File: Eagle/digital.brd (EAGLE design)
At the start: 111.1 x 67.3 mm, 53 parts, among them IC1 MAX232, J1 USB+SHIELD

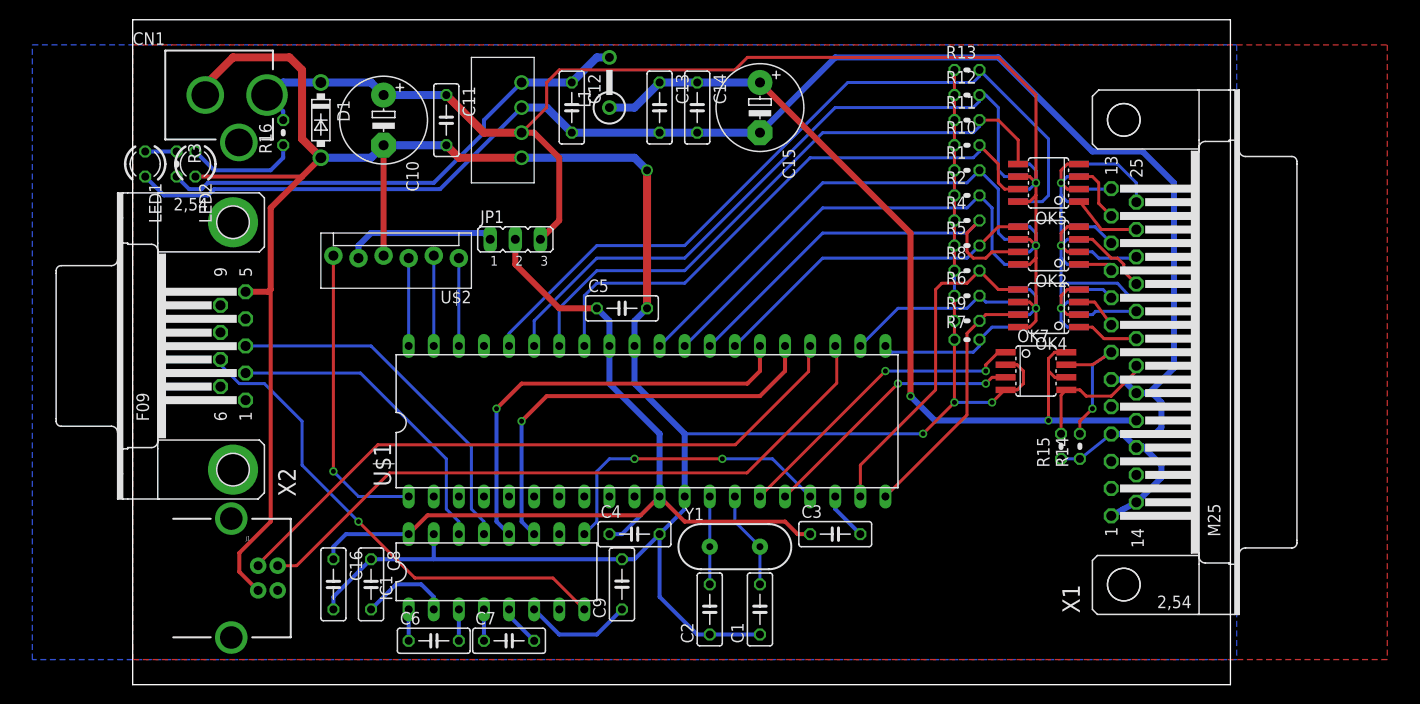
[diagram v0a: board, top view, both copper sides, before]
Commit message: Added connection monitor
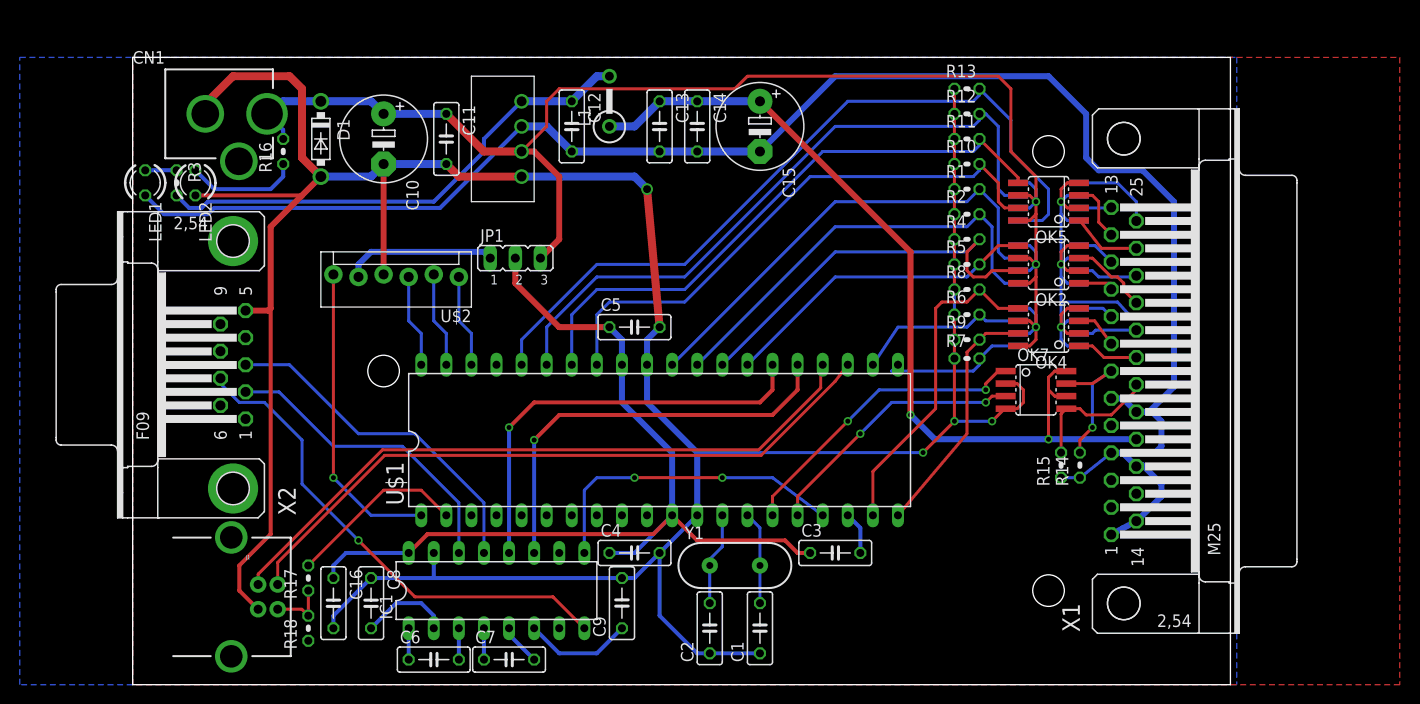
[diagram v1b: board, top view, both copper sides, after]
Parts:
- added R17, R18: 100k, resistor:0204V
- moved U$1 2.29 mm to (53.3, 24.8)
- moved C5 2.29 mm to (50.8, 36.2)
- moved C10 1.91 mm to (25.4, 55.2)
- moved C11 1.91 mm to (31.8, 55.2)
- moved C12 1.91 mm to (44.5, 56.5)
- moved C13 1.91 mm to (53.3, 56.5)
- moved C14 1.91 mm to (57.1, 56.5)
- moved C15 1.91 mm to (63.5, 56.5)
- moved CN1 1.91 mm to (0.00, 57.8)
- moved D1 1.91 mm to (19.1, 55.2)
- moved JP1 1.91 mm to (38.7, 43.2)
- moved L1 1.91 mm to (48.3, 59.1)
- moved LED1 1.91 mm to (1.27, 50.8)
- moved LED2 1.91 mm to (6.35, 50.8)
- moved OK1 1.91 mm to (92.7, 42.5)
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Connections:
- new net N$42: J1.VBUS, R17.1, R18.2
- new net N$55: R17.2, U$1.2
- net DGND: now also R18.1
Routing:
- net N$55: track 0.00 -> 18.2 mm
- net N$42: track 0.00 -> 5.91 mm
- net GND: track 228.0 -> 230.6 mm
- net N$45: track 94.2 -> 96.7 mm
- net N$4: track 30.6 -> 32.3 mm
- net N$34: track 61.8 -> 60.2 mm
- net USB_P: track 66.7 -> 68.2 mm
- net N$53: track 36.5 -> 35.0 mm
- net N$33: track 58.6 -> 57.4 mm
- net N$25: track 42.0 -> 40.7 mm
- net N$27: track 33.7 -> 32.4 mm
- net N$24: track 45.6 -> 44.3 mm
- net N$15: track 49.2 -> 47.9 mm
- net N$31: track 25.9 -> 25.0 mm
- net N$29: track 18.3 -> 17.5 mm
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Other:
- board size 111.1 x 67.3 mm -> 111.1 x 63.5 mm

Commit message: Board updates
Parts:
- moved R3 17.2 mm to (21.6, 49.5), turned to 0 degrees
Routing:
- net N$26: track 50.6 -> 31.7 mm
- net N$28: track 3.18 -> 21.5 mm
- net DGND: track 300.1 -> 293.9 mm, vias 4 -> 3
- net +5V/2: track 156.0 -> 153.7 mm
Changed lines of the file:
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@@
 <element name="C11" library="resistor" package="C050-025X075" value="0.1uF" x="31.75" y="55.245" rot="R270"/>
 <element name="U$3" library="modEEG" package="SIP4" value="ROL-0505S" x="38.1" y="55.245" rot="R90"/>
-<element name="R3" library="resistor" package="0204V" value="1.65k" x="4.445" y="50.8" rot="R270"/>
+<element name="R3" library="resistor" package="0204V" value="1.65k" x="21.59" y="49.53"/>
 <element name="LED1" library="led" package="LED3MM" value="" x="1.27" y="50.8" rot="R270"/>
 <element name="C12" library="resistor" package="C050-025X075" value="0.1uF" x="44.45" y="56.515" rot="R270"/>
@@
 <contactref element="R3" pad="1"/>
 <contactref element="LED1" pad="A"/>
-<wire x1="1.27" y1="52.07" x2="4.445" y2="52.07" width="0.4064" layer="16"/>
+<wire x1="20.32" y1="49.53" x2="8.255" y2="49.53" width="0.4064" layer="16"/>
+<wire x1="8.255" y1="49.53" x2="6.985" y2="48.26" width="0.4064" layer="16"/>
+<wire x1="6.985" y1="48.26" x2="4.445" y2="48.26" width="0.4064" layer="16"/>
+<wire x1="4.445" y1="48.26" x2="2.54" y2="50.165" width="0.4064" layer="16"/>
+<wire x1="2.54" y1="50.165" x2="2.54" y2="50.8" width="0.4064" layer="16"/>
+<wire x1="2.54" y1="50.8" x2="1.27" y2="52.07" width="0.4064" layer="16"/>
 </signal>
 <signal name="DGND">
@@
 <wire x1="31.75" y1="52.705" x2="33.02" y2="51.435" width="0.8128" layer="1"/>
 <wire x1="33.02" y1="51.435" x2="39.37" y2="51.435" width="0.8128" layer="1"/>
-<wire x1="39.37" y1="51.435" x2="50.8" y2="51.435" width="0.8128" layer="16"/>
-<wire x1="50.8" y1="51.435" x2="52.07" y2="50.165" width="0.8128" layer="16"/>
-<via x="52.07" y="50.165" extent="1-16" drill="0.8"/>
-<wire x1="52.07" y1="50.165" x2="53.34" y2="36.195" width="0.8128" layer="1"/>
+<wire x1="53.34" y1="37.465" x2="53.34" y2="36.195" width="0.8128" layer="1"/>
 <contactref element="R8" pad="1"/>
 <contactref element="R9" pad="1"/>
@@
 <wire x1="20.32" y1="6.985" x2="24.13" y2="10.795" width="0.4064" layer="16"/>
 <contactref element="R18" pad="1"/>
+<wire x1="39.37" y1="51.435" x2="53.34" y2="37.465" width="0.8128" layer="1"/>
+<wire x1="10.795" y1="12.065" x2="9.9822" y2="14.9098" width="0" layer="19" extent="1-1"/>
+<wire x1="17.78" y1="4.445" x2="20.32" y2="5.715" width="0" layer="19" extent="1-1"/>
+<wire x1="9.9822" y1="2.8702" x2="12.7" y2="7.64" width="0" layer="19" extent="1-1"/>
 </signal>
 <signal name="N$26">
@@
 <wire x1="35.56" y1="55.245" x2="35.56" y2="53.975" width="0.4064" layer="16"/>
 <wire x1="35.56" y1="53.975" x2="30.48" y2="48.895" width="0.4064" layer="16"/>
-<wire x1="4.445" y1="49.53" x2="5.715" y2="48.26" width="0.4064" layer="16"/>
-<wire x1="5.715" y1="48.26" x2="6.985" y2="48.26" width="0.4064" layer="16"/>
-<wire x1="6.985" y1="48.26" x2="7.62" y2="48.895" width="0.4064" layer="16"/>
-<wire x1="7.62" y1="48.895" x2="30.48" y2="48.895" width="0.4064" layer="16"/>
+<wire x1="30.48" y1="48.895" x2="23.495" y2="48.895" width="0.4064" layer="16"/>
+<wire x1="23.495" y1="48.895" x2="22.86" y2="49.53" width="0.4064" layer="16"/>
 </signal>
 <signal name="+5V/2">
@@
 <wire x1="41.91" y1="59.055" x2="41.91" y2="56.515" width="0.3048" layer="1"/>
 <wire x1="41.91" y1="56.515" x2="39.37" y2="53.975" width="0.3048" layer="1"/>
-<wire x1="39.37" y1="53.975" x2="40.64" y2="53.975" width="0.6096" layer="1"/>
-<wire x1="40.64" y1="53.975" x2="43.18" y2="51.435" width="0.6096" layer="1"/>
-<wire x1="43.18" y1="51.435" x2="43.18" y2="45.085" width="0.6096" layer="1"/>
-<wire x1="43.18" y1="45.085" x2="41.275" y2="43.18" width="0.6096" layer="1"/>
 <wire x1="15.24" y1="55.245" x2="15.24" y2="56.145" width="0.4064" layer="16"/>
 <wire x1="15.24" y1="56.145" x2="13.6" y2="57.785" width="0.4064" layer="16"/>
+<wire x1="39.37" y1="53.975" x2="41.275" y2="52.07" width="0.6096" layer="16"/>
+<wire x1="41.275" y1="52.07" x2="41.275" y2="43.18" width="0.6096" layer="16"/>
 </signal>
 <signal name="N$10">
